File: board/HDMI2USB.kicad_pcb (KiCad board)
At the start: 10 copper layers, 215 x 155 mm, 460 parts, among them CON1 BARREL_JACK, CON2 BARREL_JACK, J1 USB_MICRO_B, J2 HDMI, J3 HDMI, J4 HDMI, J5 HDMI, J6 RJ45(HFJ11-1GO1ERL), J7 USB_MICRO_B, J8 DISPLAY_PORT, J9 DISPLAY_PORT, P1 CONN_2, P10 CONN_1, P11 CONN_1, P12 CONN_1, P13 CONN_1, P2 CONN_1, P3 CONN_7X2, P4 CONN_1, P5 CONN_1, P6 CONN_1, P7 CONN_1, P8 CONN_1, P9 CONN_1, SW1 SW_PUSH, U1 MT41J128M16, U10 XC6SLX150T, U11 MICRO_SD, U12 TPS51200, U13 IP4776CZ38, U14 IP4776CZ38, U15 IP4776CZ38, U16 ΜA78L00, U17 FXO-HC536R, U18 USB3340, U19 MCP1825, U2 CY7C68013A_100AC, U20 RTL8211E-VB, U21 IP4776CZ38, U22 ΜA78L00, U23 24AA02E48, U3 W25Q128FVEIG, U4 GBU15005-G, U5 7805, U6 TPS54560, U7 TPS53319, U8 TPS54625, U9 TPS54625, X1 CRYSTAL, X2 50MHz

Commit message: Issue #1608 - Placement
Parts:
- moved R191 14.5 mm to (146.6, 193.8)
- moved C104 11.1 mm to (208.9, 167.5)
- moved R124 8.38 mm to (148.3, 197.2)
- moved R125 8.38 mm to (146.3, 197.2)
- moved R131 8.38 mm to (144.2, 197.2)
- moved R30 6.85 mm to (210.8, 94.2), turned to 0 degrees
- moved J8 5.84 mm to (231.9, 219.1)
- moved R126 3.81 mm to (151.8, 204.3)
- moved R129 3.81 mm to (151.8, 200.5)
- moved R133 3.81 mm to (151.8, 198.4)
- moved R127 2.79 mm to (128.7, 201.0)
- moved R130 2.79 mm to (126.7, 201.0)
- moved R134 2.79 mm to (124.7, 201.0)
- moved R188 2.79 mm to (120.9, 200.2)
- moved R189 2.79 mm to (120.9, 198.2)
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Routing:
- net /Power/VIN 48: track 0.00 -> 101.5 mm
- net /FPGA_Bank_0_3/TXHPD: track 77.6 -> 0.00 mm, vias 1 -> 0
- net /FPGA_Bank_0_3/USB_REFCLK: track 1.57 -> 74.6 mm
- net /Power/VIN +48V: track 0.00 -> 68.7 mm
- net /HDMI/TMDS-RX1-CLK_N: track 56.3 -> 119.8 mm
- net /HDMI/TMDS-RX1-1_N: track 56.2 -> 119.6 mm
- net /HDMI/TMDS-RX1-CLK_P: track 57.9 -> 119.5 mm
- net /HDMI/TMDS-RX1-1_P: track 58.6 -> 119.6 mm
- net /HDMI/TMDS-RX1-0_P: track 58.9 -> 119.6 mm
- net /FPGA_Bank_0_3/USB_D7: track 2.01 -> 62.5 mm
- net /HDMI/TMDS-RX1-0_N: track 60.2 -> 119.5 mm
- net /HDMI/TMDS-RX1-2_N: track 61.6 -> 119.6 mm
- net /HDMI/TMDS-RX1-2_P: track 62.1 -> 119.7 mm
- net /Power/VIN -48V: track 0.00 -> 45.1 mm
- net /HDMI/TMDS-RX2-2_N: track 77.8 -> 119.7 mm
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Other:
- outline, holes or cut-outs redrawn

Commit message: Issue #1412 - Placement
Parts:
- added U24: BDXXGA5WEFJ_, 8-HTSOP-J_(BD50GA5WEFJ-E2), F.Cu at (197.0, 100.7)
- added U25: TIMVIDEOS-PCIE-8X, PCIe_98Pos, F.Cu at (109.7, 37.7)
- moved U3 216.6 mm to (161.2, 163.1)
- moved R36 192.7 mm to (209.3, 224.0)
- moved R22 182.0 mm to (61.7, 172.2)
- moved C203 182.0 mm to (65.8, 175.0)
- moved C204 182.0 mm to (68.4, 175.0)
- moved R38 182.0 mm to (72.9, 172.7)
- moved R39 182.0 mm to (72.9, 169.9)
- moved U19 182.0 mm to (67.1, 166.9)
- moved C36 161.5 mm to (161.2, 171.4)
- moved R21 161.5 mm to (161.8, 169.2)
- moved C228 152.5 mm to (89.5, 166.8)
- moved C211 152.5 mm to (77.8, 166.8)
- moved C212 152.5 mm to (80.3, 172.1)
- moved C217 152.5 mm to (80.3, 161.7)
- moved C218 152.5 mm to (80.3, 166.8)
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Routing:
- net /Power/VIN 48: track 101.5 -> 0.00 mm
- net (no net): track 426.5 -> 510.8 mm, vias 62 -> 92
- net GND: track 533.4 -> 469.2 mm, vias 222 -> 202
- net /SPI_Flash/TDO-FPGA/TDO-JTAG: track 80.0 -> 21.9 mm
- net /FPGA_Power/TCK: track 34.1 -> 10.4 mm
- net /SPI_Flash/TDO-USB/TDI-FPGA: track 40.9 -> 17.5 mm
- net /FPGA_Power/TMS: track 36.4 -> 14.1 mm
- net /HDMI/TMDS-RX2-1_P: track 102.0 -> 119.6 mm
- net /Ethernet/ETH_TXD1: track 127.3 -> 143.6 mm
- net /Ethernet/ETH_TXD3: track 127.5 -> 143.6 mm
- net /USB/ID: track 14.3 -> 29.7 mm
- net /Ethernet/ETH_TXD0: track 128.5 -> 143.5 mm
- net /Ethernet/ETH_TXD2: track 128.8 -> 143.5 mm
- net /Ethernet/ETH_TXCTL: track 128.9 -> 143.6 mm
- net /Ethernet/ETH_RXCTL: track 157.8 -> 143.5 mm
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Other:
- board size 215 x 155 mm -> 215 x 135 mm

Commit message: Issue #1412 - Placement on 6-3-15
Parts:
- added 1PIN: P***, MH-4MM, F.Cu at (96.0, 216.0)
- added 1PIN: P***, MH-4MM, F.Cu at (295.0, 224.0)
- added 1PIN: P***, MH-4MM, F.Cu at (284.0, 100.0)
- added 1PIN: P***, MH-4MM, F.Cu at (96.0, 93.0)
- U5: value 7805 -> 7805_N
- moved U25 203.7 mm to (262.1, 172.9), turned to 90 degrees
- moved R92 169.0 mm to (134.4, 67.2), turned to 0 degrees
- moved R89 158.7 mm to (114.0, 66.7), turned to 180 degrees
- moved J6 154.2 mm to (124.0, 71.3), turned to 180 degrees
- moved R72 131.0 mm to (135.2, 88.9), turned to 0 degrees
- moved C235 128.2 mm to (139.7, 93.6), turned to 0 degrees
- moved C238 120.1 mm to (139.7, 98.7), turned to 0 degrees
- moved X2 119.6 mm to (135.9, 96.2), turned to 270 degrees
- moved C233 117.7 mm to (125.0, 91.1), turned to 90 degrees
- moved C234 115.9 mm to (122.7, 91.1), turned to 90 degrees
- moved C203 114.7 mm to (156.2, 104.5)
- moved C223 114.7 mm to (177.3, 101.6)
- moved R38 114.7 mm to (163.3, 102.2)
- moved C204 114.7 mm to (158.8, 104.5)
- moved C210 114.7 mm to (168.2, 91.2)
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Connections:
- U5 pad 1: (no net) -> N-00000393
- U5 pad 2: (no net) -> GND
- U5 pad 3: (no net) -> VCC5V0
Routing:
- net /Ethernet/ETH_RXD3: track 143.5 -> 12.5 mm
- net /Ethernet/ETH_RXD2: track 143.6 -> 20.0 mm
- net /Ethernet/ETH_RXD1: track 143.5 -> 25.7 mm
- net /Ethernet/ETH_RXD0: track 143.5 -> 28.1 mm
- net /Ethernet/ETH_MDC: track 133.7 -> 29.3 mm
- net /Ethernet/ETH_RXCTL: track 143.5 -> 40.0 mm
- net /Ethernet/ETH_MDIO: track 135.8 -> 32.6 mm
- net /Ethernet/ETH_RESET_B: track 136.4 -> 33.5 mm
- net /Ethernet/ETH_TXCTL: track 143.6 -> 41.1 mm
- net /FPGA_Bank_1_2/SD_DAT2: track 122.5 -> 38.3 mm
- net /FPGA_Bank_1_2/SD_CLK: track 126.6 -> 42.4 mm
- net /FPGA_Bank_1_2/SD_DAT3: track 123.1 -> 39.1 mm
- net /FPGA_Bank_1_2/SD_CMD: track 129.0 -> 45.0 mm
- net /FPGA_Bank_1_2/SD_DAT1: track 122.2 -> 38.5 mm
- net /FPGA_Bank_1_2/SD_DAT0: track 125.4 -> 41.8 mm
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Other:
- board size 215 x 135 mm -> 203 x 170 mm

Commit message: Issue #1605 - Cypress routing
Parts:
- U11: moved to B.Cu
- moved U11 60.2 mm to (105.1, 123.4), turned to 270 degrees
- moved C141 53.2 mm to (162.8, 88.0)
- moved C144 53.2 mm to (156.9, 88.2)
- moved C158 53.2 mm to (162.2, 86.4)
- moved C164 53.2 mm to (153.1, 94.1)
- moved C167 53.2 mm to (153.1, 94.1)
- moved R103 53.2 mm to (157.7, 88.2)
- moved R104 53.2 mm to (160.0, 87.2)
- moved R114 53.2 mm to (160.5, 86.4)
- moved R115 53.2 mm to (164.0, 86.4)
- moved U9 53.2 mm to (161.2, 93.3)
- moved C152 53.2 mm to (163.0, 100.9)
- moved C80 53.2 mm to (166.1, 100.2)
- moved C134 53.2 mm to (167.3, 94.8)
- moved C139 53.2 mm to (171.1, 94.8)
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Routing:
- net /Ethernet/ETH_TXCLK: track 0.68 -> 119.1 mm, vias 1 -> 2
- net /Ethernet/ETH_RXD3: track 12.5 -> 119.2 mm
- net /Ethernet/ETH_RXD2: track 20.0 -> 119.2 mm
- net /Ethernet/ETH_RXD1: track 25.7 -> 119.2 mm
- net /Ethernet/ETH_RXD0: track 28.1 -> 119.2 mm
- net /Ethernet/ETH_RXCTL: track 40.0 -> 119.2 mm
- net /Ethernet/ETH_TXCTL: track 41.1 -> 119.1 mm
- net /HDMI/TMDS-TX1-CLK_N: track 59.8 -> 124.9 mm
- net /HDMI/TMDS-TX1-0_N: track 60.7 -> 124.8 mm
- net /HDMI/TMDS-TX1-0_P: track 61.5 -> 124.8 mm
- net /HDMI/TMDS-TX1-CLK_P: track 61.7 -> 124.8 mm
- net /HDMI/TMDS-RX2-2_N: track 61.9 -> 124.9 mm
- net /Ethernet/ETH_RESET_B: track 33.5 -> 94.9 mm
- net /HDMI/TMDS-RX2-2_P: track 63.8 -> 124.8 mm
- net /Ethernet/ETH_MDC: track 29.3 -> 90.0 mm
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
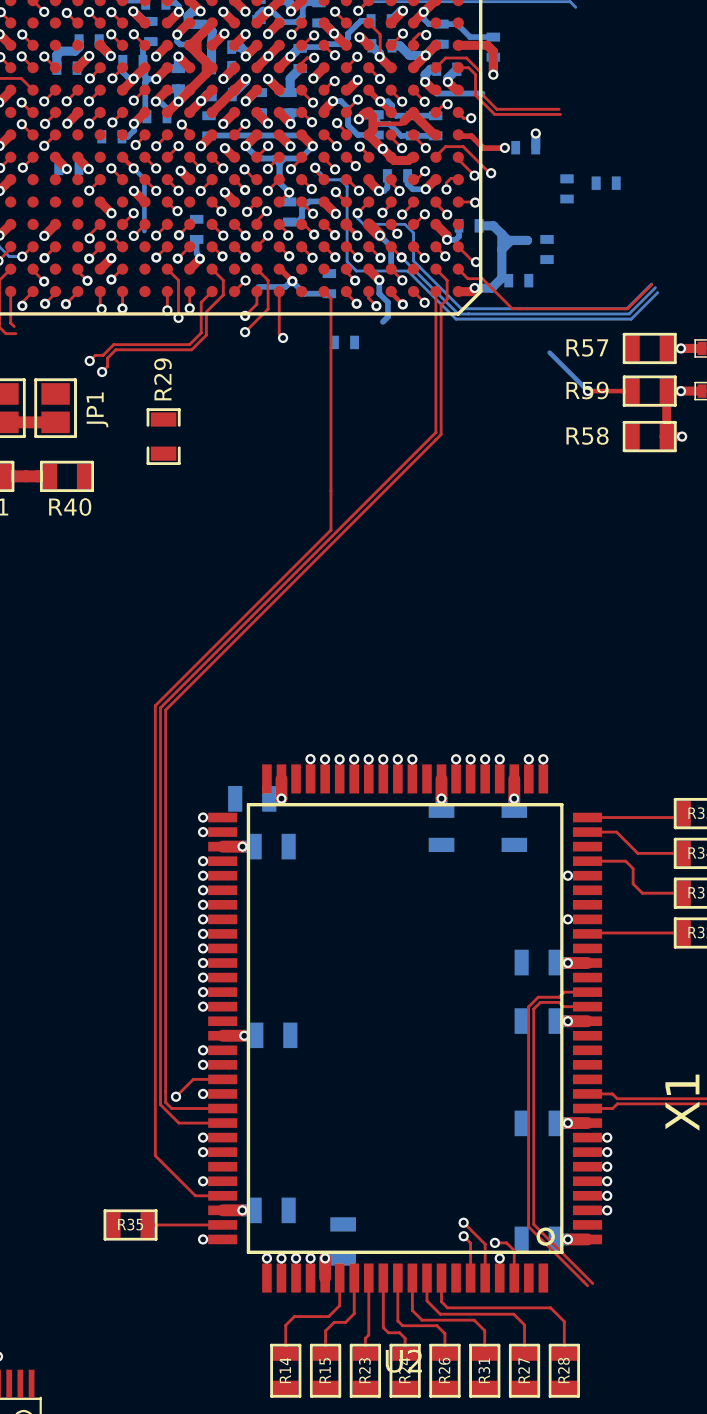
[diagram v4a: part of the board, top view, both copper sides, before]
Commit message: Issue #1605 - Cypress routing
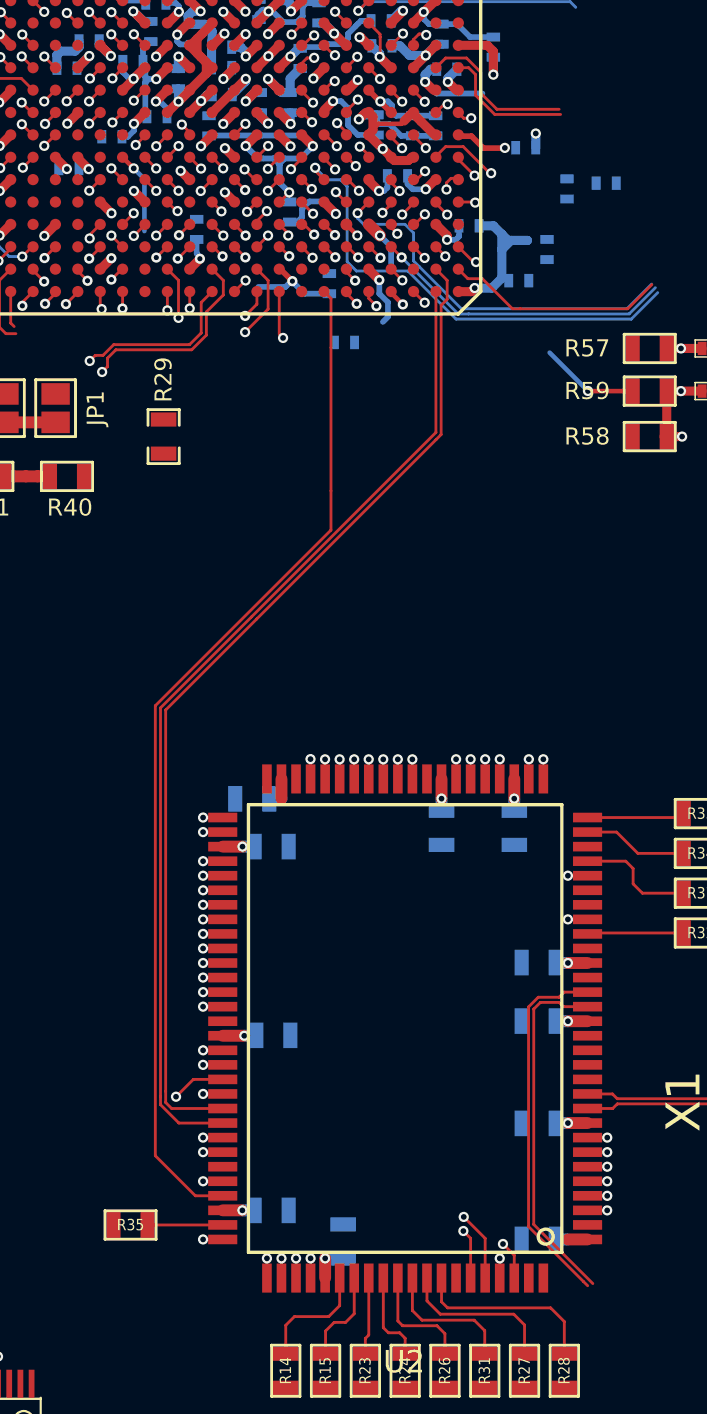
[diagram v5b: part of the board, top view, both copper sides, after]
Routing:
- net /FPGA_Bank_1_2/CY_FD1: track 23.1 -> 62.3 mm
- net /FPGA_Bank_1_2/CY_FD0: track 25.4 -> 62.3 mm
- net /FPGA_Bank_1_2/CY_FD3: track 34.5 -> 62.3 mm
- net /FPGA_Bank_1_2/CY_FD2: track 37.4 -> 62.3 mm
- net /FPGA_Bank_1_2/CY_FD11: track 46.5 -> 62.3 mm
- net /FPGA_Bank_1_2/CY_FD10: track 47.5 -> 62.4 mm
- net /FPGA_Bank_1_2/CY_RD4: track 72.9 -> 86.5 mm
- net /FPGA_Bank_1_2/CY_RD5: track 73.2 -> 86.5 mm
- net /FPGA_Bank_1_2/CY_FD9: track 49.9 -> 62.4 mm
- net /FPGA_Bank_1_2/CY_RD1: track 75.1 -> 86.5 mm
- net /FPGA_Bank_1_2/CY_FD8: track 52.1 -> 62.3 mm
- net /FPGA_Bank_1_2/CY_PA7: track 49.6 -> 59.6 mm
- net /FPGA_Bank_1_2/CY_PA6: track 50.0 -> 60.0 mm
- net /FPGA_Bank_1_2/CY_FD13: track 54.6 -> 62.3 mm
- net /FPGA_Bank_1_2/CY_TXD1: track 49.6 -> 42.0 mm
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
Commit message: Issue #1683
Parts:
- moved C111 0.63 mm to (206.7, 155.3)
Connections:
- C151 pad 2: N-00000400 -> N-00000348
- C154 pad 2: N-00000400 -> N-00000348
- J8 pad 18: /FPGA_Bank_0_3/TXHPD -> /FPGA_Bank_1_2/TXHPD
- J9 pad 18: /FPGA_Bank_0_3/RXHPD -> /FPGA_Bank_1_2/RXHPD
- R109 pad 1: N-00000400 -> N-00000348
- R37 pad 1: N-00000348 -> N-00000280
- U10 pad A17: (no net) -> /FPGA_Bank_0_3/DIFFIO_B2N
- U10 pad A18: /DisplayPort/RXCONFIG1 -> /FPGA_Bank_0_3/DIFFIO_A1N
- U10 pad A19: /FPGA_Bank_0_3/TXHPD -> /FPGA_Bank_0_3/DIFFIO_XN
- U10 pad A2: /FPGA_Bank_0_3/USB_D3 -> /FPGA_Bank_0_3/DIFFIO_A6N
- U10 pad A20: /DisplayPort/TXAUXCH_N -> /FPGA_Bank_0_3/DIFFIO_B0N
- U10 pad A3: /FPGA_Bank_0_3/USB_RESETB -> /FPGA_Bank_0_3/DIFFIO_B6N
- U10 pad A4: /FPGA_Bank_0_3/USB_DIR -> /FPGA_Bank_0_3/DIFFIO_A5N
- U10 pad A5: (no net) -> /FPGA_Bank_0_3/DIFFIO_B5N
- U10 pad AA14: (no net) -> /FPGA_Bank_1_2/USB_D4
- U10 pad AA8: /HDMI/TMDS-TX1-SCL -> /DisplayPort/RXCONFIG1
- U10 pad AB14: (no net) -> /FPGA_Bank_1_2/USB_D5
- U10 pad AB8: /HDMI/TMDS-TX1-SDA -> /DisplayPort/RXCONFIG2
- U10 pad B18: /DisplayPort/RXCONFIG2 -> /FPGA_Bank_0_3/DIFFIO_A1P
- U10 pad B2: /FPGA_Bank_0_3/USB_D4 -> /FPGA_Bank_0_3/DIFFIO_A6P
- U10 pad B20: /DisplayPort/TXAUXCH_P -> /FPGA_Bank_0_3/DIFFIO_B0P
- U10 pad B3: /FPGA_Bank_0_3/USB_D0 -> /FPGA_Bank_0_3/DIFFIO_B6P
- U10 pad C1: (no net) -> /Ethernet/MAC_SDA
- U10 pad C17: (no net) -> /FPGA_Bank_0_3/DIFFIO_B2P
- U10 pad C18: /DisplayPort/TXCONFIG1 -> /FPGA_Bank_0_3/DIFFIO_A0N
- U10 pad C19: /FPGA_Bank_0_3/RXHPD -> /FPGA_Bank_0_3/DIFFIO_XP
- U10 pad C4: /FPGA_Bank_0_3/USB_STP -> /FPGA_Bank_0_3/DIFFIO_A5P
- U10 pad C5: (no net) -> /FPGA_Bank_0_3/DIFFIO_B5P
- U10 pad D17: /DisplayPort/TXCONFIG2 -> /FPGA_Bank_0_3/DIFFIO_A0P
- U10 pad D18: /DisplayPort/RXAUXCH_P -> /FPGA_Bank_0_3/DIFFCLK_XP
- U10 pad D19: /DisplayPort/RXAUXCH_N -> /FPGA_Bank_0_3/DIFFCLK_XN
- U10 pad D3: /FPGA_Bank_0_3/USB_D7 -> /FPGA_Bank_0_3/PCIE_RESET
- U10 pad D4: /FPGA_Bank_0_3/USB_D6 -> /FPGA_Bank_0_3/DIFFIO_B4P
- U10 pad D5: /FPGA_Bank_0_3/USB_D5 -> /FPGA_Bank_0_3/DIFFIO_B4N
- U10 pad E16: (no net) -> /FPGA_Bank_0_3/DIFFCLK_B0N
- U10 pad E5: /FPGA_Bank_0_3/USB_D2 -> /FPGA_Bank_0_3/DIFFIO_A4P
- U10 pad E6: /FPGA_Bank_0_3/USB_D1 -> /FPGA_Bank_0_3/DIFFIO_A4N
- U10 pad F10: (no net) -> /FPGA_Bank_0_3/DIFFCLK_A1P
- U10 pad F14: (no net) -> /FPGA_Bank_0_3/DIFFCLK_A0P
- U10 pad F15: (no net) -> /FPGA_Bank_0_3/DIFFCLK_A0N
- U10 pad F16: (no net) -> /FPGA_Bank_0_3/DIFFCLK_B0P
- U10 pad F17: (no net) -> /FPGA_Bank_0_3/DIFFIO_B1N
- U10 pad F7: /FPGA_Bank_0_3/USB_NXT -> /FPGA_Bank_0_3/DIFFIO_YP
- U10 pad F8: (no net) -> /FPGA_Bank_0_3/DIFFIO_YN
- U10 pad F9: (no net) -> /FPGA_Bank_0_3/DIFFIO_ZN
- U10 pad G11: (no net) -> /FPGA_Bank_0_3/DIFFCLK_B1N
- U10 pad G13: (no net) -> /FPGA_Bank_0_3/DIFFIO_A3N
- U10 pad G15: (no net) -> /FPGA_Bank_0_3/DIFFIO_A2N
- U10 pad G16: (no net) -> /FPGA_Bank_0_3/DIFFIO_B1P
- U10 pad G6: (no net) -> /Ethernet/MAC_SCL
- U10 pad G8: (no net) -> /FPGA_Bank_0_3/DIFFIO_ZP
- U10 pad G9: /FPGA_Bank_0_3/USB_REFCLK -> /FPGA_Bank_0_3/DIFFCLK_A1N
- U10 pad H10: (no net) -> /FPGA_Bank_0_3/DIFFIO_B3P
- U10 pad H11: (no net) -> /FPGA_Bank_0_3/DIFFIO_B3N
- U10 pad H12: (no net) -> /FPGA_Bank_0_3/DIFFCLK_B1P
- U10 pad H13: (no net) -> /FPGA_Bank_0_3/DIFFIO_A3P
- U10 pad H14: (no net) -> /FPGA_Bank_0_3/DIFFIO_A2P
- U10 pad H21: /HDMI/TMDS-RX1-SCL -> /HDMI/TMDS-RX1-2_P
- U10 pad H22: /HDMI/TMDS-RX1-SDA -> /HDMI/TMDS-RX1-2_N
- U10 pad J20: /HDMI/TMDS-RX1-1_P -> /HDMI/TMDS-RX1-0_P
- U10 pad J22: /HDMI/TMDS-RX1-1_N -> /HDMI/TMDS-RX1-0_N
- U10 pad K17: /HDMI/TMDS-RX2-HOT -> /HDMI/TMDS-RX1-SCL
- U10 pad K20: /HDMI/TMDS-RX1-2_P -> /HDMI/TMDS-RX1-1_P
- U10 pad K21: /HDMI/TMDS-RX1-CLK_P -> (no net)
- U10 pad K22: /HDMI/TMDS-RX1-CLK_N -> (no net)
- U10 pad L17: /HDMI/TMDS-RX1-CEC -> /HDMI/TMDS-RX1-SDA
- U10 pad L19: /HDMI/TMDS-RX1-2_N -> /HDMI/TMDS-RX1-1_N
- U10 pad M19: /HDMI/TMDS-RX1-0_N -> /HDMI/TMDS-RX1-CLK_N
- U10 pad M20: /HDMI/TMDS-RX1-0_P -> /HDMI/TMDS-RX1-CLK_P
- U10 pad R11: (no net) -> /DisplayPort/TXCONFIG1
- U10 pad T10: /Ethernet/MAC_SDA -> /DisplayPort/RXAUXCH_P
- U10 pad T11: (no net) -> /DisplayPort/TXCONFIG2
- U10 pad T15: (no net) -> /DisplayPort/TXAUXCH_P
- U10 pad T18: (no net) -> /HDMI/TMDS-RX2-HOT
- U10 pad U10: /Ethernet/MAC_SCL -> /DisplayPort/RXAUXCH_N
- U10 pad U15: (no net) -> /DisplayPort/TXAUXCH_N
- U10 pad U16: (no net) -> /FPGA_Bank_1_2/USB_D0
- U10 pad V11: (no net) -> /FPGA_Bank_1_2/TXHPD
- U10 pad V13: (no net) -> /FPGA_Bank_1_2/USB_NXT
- U10 pad V15: (no net) -> /FPGA_Bank_1_2/USB_D1
- U10 pad V17: (no net) -> /FPGA_Bank_1_2/USB_RESETB
- U10 pad V19: (no net) -> /HDMI/TMDS-RX1-CEC
- U10 pad W10: (no net) -> /HDMI/TMDS-TX1-SCL
- U10 pad W11: (no net) -> /FPGA_Bank_1_2/RXHPD
- U10 pad W13: (no net) -> /FPGA_Bank_1_2/USB_DIR
- U10 pad W15: (no net) -> /FPGA_Bank_1_2/USB_D7
- U10 pad W17: (no net) -> /FPGA_Bank_1_2/USB_D2
- U10 pad W18: (no net) -> /FPGA_Bank_1_2/USB_STP
- U10 pad Y10: (no net) -> /HDMI/TMDS-TX1-SDA
- U10 pad Y13: /Ethernet/ETH_FPGA_CLK -> /FPGA_Bank_1_2/USB_REFCLK
- U10 pad Y16: (no net) -> /FPGA_Bank_1_2/USB_D6
- U10 pad Y18: (no net) -> /FPGA_Bank_1_2/USB_D3
- U18 pad 10: /FPGA_Bank_0_3/USB_D6 -> /FPGA_Bank_1_2/USB_D6
- U18 pad 13: /FPGA_Bank_0_3/USB_D7 -> /FPGA_Bank_1_2/USB_D7
- U18 pad 2: /FPGA_Bank_0_3/USB_NXT -> /FPGA_Bank_1_2/USB_NXT
- U18 pad 26: /FPGA_Bank_0_3/USB_REFCLK -> /FPGA_Bank_1_2/USB_REFCLK
- U18 pad 27: /FPGA_Bank_0_3/USB_RESETB -> /FPGA_Bank_1_2/USB_RESETB
- U18 pad 29: /FPGA_Bank_0_3/USB_STP -> /FPGA_Bank_1_2/USB_STP
- U18 pad 3: /FPGA_Bank_0_3/USB_D0 -> /FPGA_Bank_1_2/USB_D0
- U18 pad 31: /FPGA_Bank_0_3/USB_DIR -> /FPGA_Bank_1_2/USB_DIR
- U18 pad 4: /FPGA_Bank_0_3/USB_D1 -> /FPGA_Bank_1_2/USB_D1
- U18 pad 5: /FPGA_Bank_0_3/USB_D2 -> /FPGA_Bank_1_2/USB_D2
- U18 pad 6: /FPGA_Bank_0_3/USB_D3 -> /FPGA_Bank_1_2/USB_D3
- U18 pad 7: /FPGA_Bank_0_3/USB_D4 -> /FPGA_Bank_1_2/USB_D4
- U18 pad 9: /FPGA_Bank_0_3/USB_D5 -> /FPGA_Bank_1_2/USB_D5
- U2 pad 27: N-00000348 -> N-00000280
- U25 pad A11: (no net) -> /FPGA_Bank_0_3/PCIE_RESET
- U25 pad A13: (no net) -> /FPGA_Bank_0_3/DIFFCLK_XP
- U25 pad A14: (no net) -> /FPGA_Bank_0_3/DIFFCLK_XN
- U25 pad A16: (no net) -> /FPGA_Bank_0_3/DIFFIO_A1P
- U25 pad A17: (no net) -> /FPGA_Bank_0_3/DIFFIO_A1N
- U25 pad A19: (no net) -> /FPGA_Bank_0_3/DIFFIO_YP
- U25 pad A21: (no net) -> /FPGA_Bank_0_3/DIFFIO_A2P
- U25 pad A22: (no net) -> /FPGA_Bank_0_3/DIFFIO_A2N
- U25 pad A25: (no net) -> /FPGA_Bank_0_3/DIFFIO_A3P
- U25 pad A26: (no net) -> /FPGA_Bank_0_3/DIFFIO_A3N
- U25 pad A29: (no net) -> /FPGA_Bank_0_3/DIFFCLK_A0P
- U25 pad A30: (no net) -> /FPGA_Bank_0_3/DIFFCLK_A0N
- U25 pad A32: (no net) -> /FPGA_Bank_0_3/DIFFIO_ZP
- U25 pad A35: (no net) -> /FPGA_Bank_0_3/DIFFIO_A4P
- U25 pad A36: (no net) -> /FPGA_Bank_0_3/DIFFIO_A4N
- U25 pad A39: (no net) -> /FPGA_Bank_0_3/DIFFIO_A5P
- U25 pad A40: (no net) -> /FPGA_Bank_0_3/DIFFIO_A5N
- U25 pad A43: (no net) -> /FPGA_Bank_0_3/DIFFIO_A6P
- U25 pad A44: (no net) -> /FPGA_Bank_0_3/DIFFIO_A6N
- U25 pad A47: (no net) -> /FPGA_Bank_0_3/DIFFCLK_A1P
- U25 pad A48: (no net) -> /FPGA_Bank_0_3/DIFFCLK_A1N
- U25 pad A5: (no net) -> /FPGA_Bank_0_3/DIFFIO_A0P
- U25 pad A6: (no net) -> /FPGA_Bank_0_3/DIFFIO_A0N
- U25 pad A7: (no net) -> /FPGA_Bank_0_3/DIFFIO_B0P
- U25 pad A8: /GPIOs/DIFFIO_B1N -> /FPGA_Bank_0_3/DIFFIO_B0N
- U25 pad B11: (no net) -> /FPGA_Bank_0_3/DIFFIO_XN
- U25 pad B12: (no net) -> /FPGA_Bank_0_3/DIFFIO_YN
- U25 pad B14: (no net) -> /FPGA_Bank_0_3/DIFFIO_B1P
- U25 pad B15: /GPIOs/DIFFIO_B1N -> /FPGA_Bank_0_3/DIFFIO_B1N
- U25 pad B19: (no net) -> /FPGA_Bank_0_3/DIFFIO_B2P
- U25 pad B20: (no net) -> /FPGA_Bank_0_3/DIFFIO_B2N
- U25 pad B23: (no net) -> /FPGA_Bank_0_3/DIFFIO_B3P
- U25 pad B24: (no net) -> /FPGA_Bank_0_3/DIFFIO_B3N
- U25 pad B27: (no net) -> /FPGA_Bank_0_3/DIFFCLK_B0P
- U25 pad B28: (no net) -> /FPGA_Bank_0_3/DIFFCLK_B0N
- U25 pad B30: (no net) -> /FPGA_Bank_0_3/DIFFIO_ZN
- U25 pad B33: (no net) -> /FPGA_Bank_0_3/DIFFIO_B4P
- U25 pad B34: (no net) -> /FPGA_Bank_0_3/DIFFIO_B4N
- U25 pad B37: (no net) -> /FPGA_Bank_0_3/DIFFIO_B5P
- U25 pad B38: (no net) -> /FPGA_Bank_0_3/DIFFIO_B5N
- U25 pad B41: (no net) -> /FPGA_Bank_0_3/DIFFIO_B6P
- U25 pad B42: (no net) -> /FPGA_Bank_0_3/DIFFIO_B6N
- U25 pad B45: (no net) -> /FPGA_Bank_0_3/DIFFCLK_B1P
- U25 pad B46: (no net) -> /FPGA_Bank_0_3/DIFFCLK_B1N
- U25 pad B9: (no net) -> /FPGA_Bank_0_3/DIFFIO_XP
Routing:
- net (no net): track 417.7 -> 180.5 mm, vias 62 -> 31
- net /FPGA_Bank_0_3/PCIE_RESET: track 0.00 -> 99.1 mm, vias 0 -> 1
- net /FPGA_Bank_0_3/DIFFIO_YN: track 0.00 -> 92.5 mm, vias 0 -> 1
- net /FPGA_Bank_0_3/DIFFIO_YP: track 0.00 -> 86.5 mm, vias 0 -> 1
- net /FPGA_Bank_0_3/DIFFCLK_A0N: track 0.00 -> 86.1 mm, vias 0 -> 1
- net /HDMI/TMDS-RX1-2_N: track 124.8 -> 39.5 mm, vias 2 -> 1
- net /FPGA_Bank_0_3/USB_D2: track 83.4 -> 0.00 mm, vias 2 -> 0
- net /FPGA_Bank_0_3/USB_D6: track 82.6 -> 0.00 mm, vias 2 -> 0
- net /FPGA_Bank_0_3/USB_D5: track 82.1 -> 0.00 mm, vias 2 -> 0
- net /FPGA_Bank_0_3/USB_REFCLK: track 81.7 -> 0.00 mm, vias 2 -> 0
- net /FPGA_Bank_0_3/DIFFCLK_A0P: track 0.00 -> 81.6 mm, vias 0 -> 1
- net /FPGA_Bank_0_3/USB_D7: track 81.3 -> 0.00 mm, vias 2 -> 0
- net /FPGA_Bank_0_3/USB_D1: track 80.5 -> 0.00 mm, vias 2 -> 0
- net /FPGA_Bank_0_3/USB_NXT: track 78.7 -> 0.00 mm, vias 2 -> 0
- net /HDMI/TMDS-RX1-2_P: track 124.9 -> 47.7 mm, vias 2 -> 1
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- added copper zone on F.Cu, net N-00000391
- added copper zone on F.Cu, net N-00000398
- added copper zone on F.Cu, net N-00000401
- removed copper zone on F.Cu, net N-00000332
- removed copper zone on F.Cu, net N-00000349
- removed copper zone on F.Cu, net N-00000363
